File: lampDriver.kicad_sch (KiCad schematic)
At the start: 49 parts, among them IC8 FAN3100TSX, T4 NMOS_GDS-KS_SMD, U1 OPA2356AIDGKR, U3 LM2903, U4 AZ431LANTR

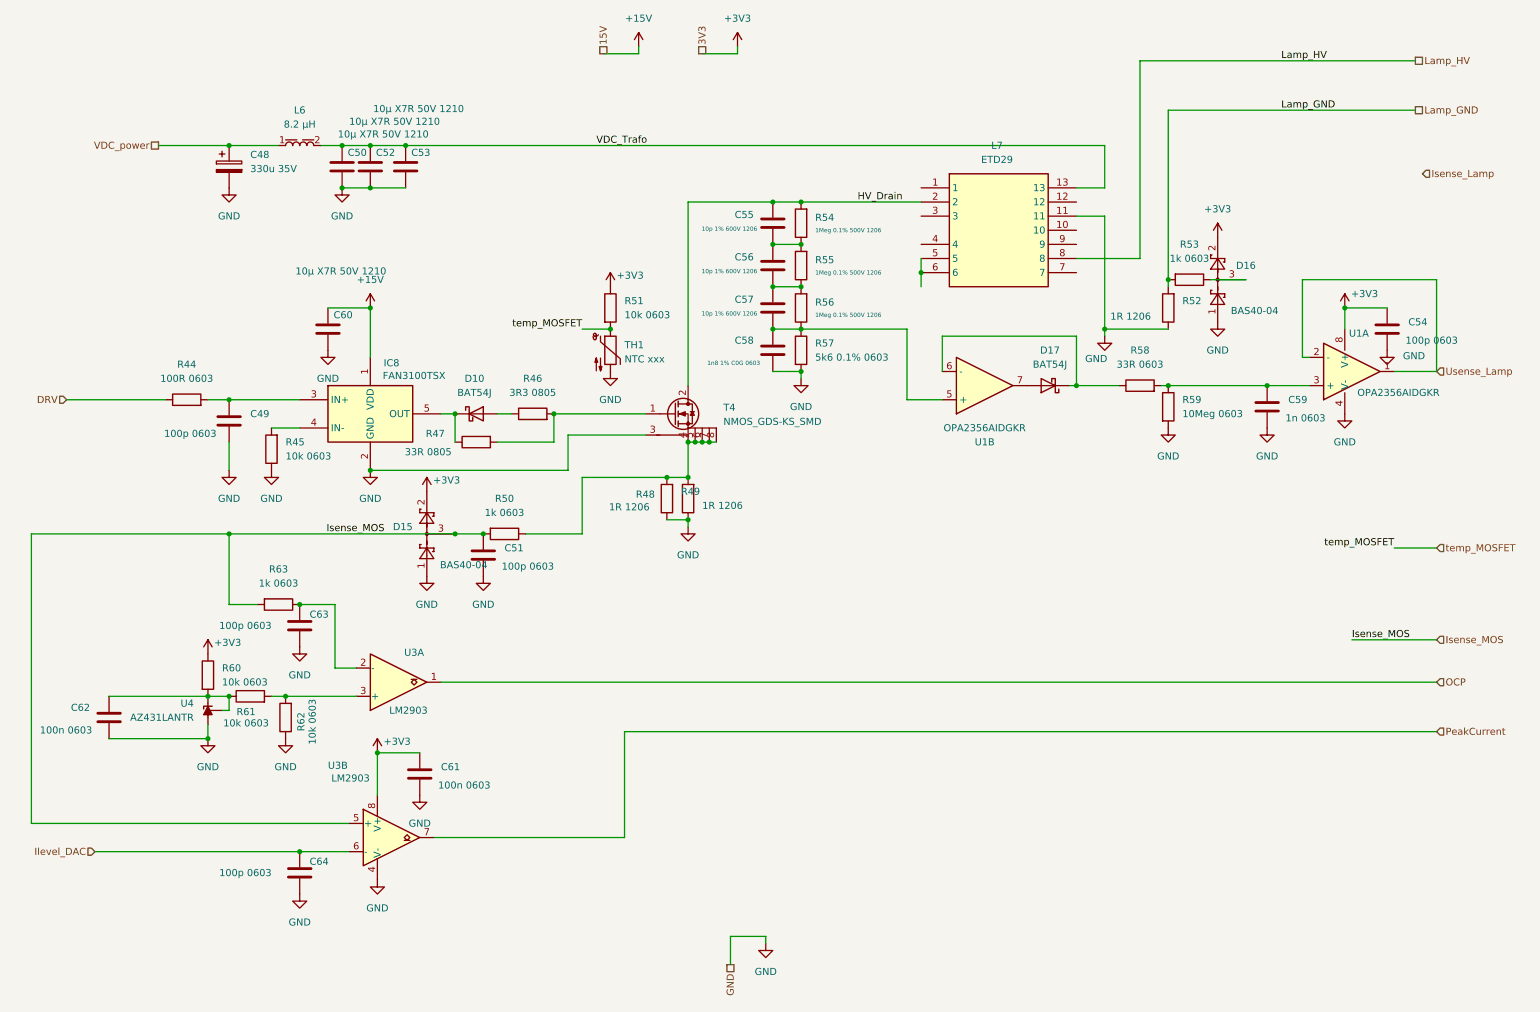
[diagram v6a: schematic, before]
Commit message: new current control V1
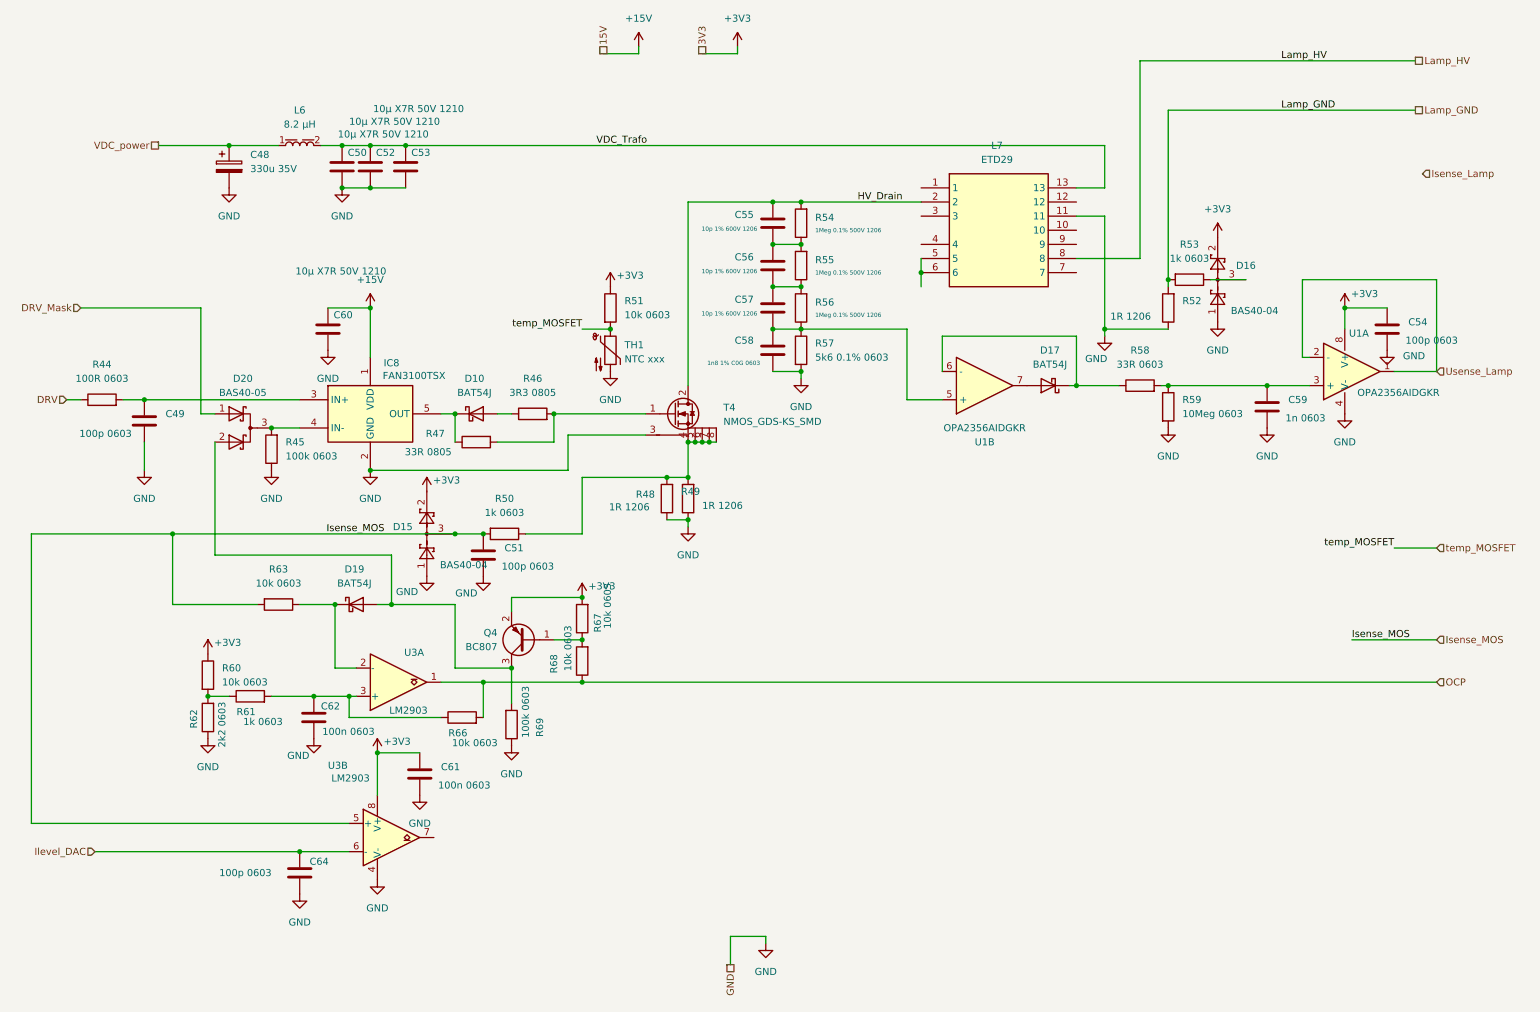
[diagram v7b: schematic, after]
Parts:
- removed C63: 100p 0603, Capacitor_SMD:C_0603_1608Metric, symbol Device:C
- removed U4: AZ431LANTR, Package_TO_SOT_SMD:SOT-23, symbol Reference_Voltage:TL432DBZ
- added D19: BAT54J, Diode_SMD:D_SOD-323F, symbol Diode:BAT54J
- added D20: BAS40-05, Package_TO_SOT_SMD:SOT-23, symbol Device:D_Schottky_Dual_CommonCathode_AAK_Parallel
- added Q4: BC807, Package_TO_SOT_SMD:SOT-23, symbol Transistor_BJT:Q_PNP_BEC
- added R66, R67, R68: 10k 0603, Resistor_SMD:R_0603_1608Metric, symbol Device:R
- added R69: 100k 0603, Resistor_SMD:R_0603_1608Metric, symbol Device:R
- R45: value 10k 0603 -> 100k 0603
- R61: value 10k 0603 -> 1k 0603
- R62: value 10k 0603 -> 2k2 0603
- R63: value 1k 0603 -> 10k 0603
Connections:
- net +3V3: now also Q4.2 (E), R67.2
- net GND: now also R69.1
- net OCP: now also R66.2, R68.1
- net at IC8.4 (IN-), R45.2: now also D20.3 (K)
- net at R60.2, R61.1: now also R62.2; no longer C62.1
- net at R61.2, U3.3 (+): now also C62.1, R66.1; no longer R62.2
- net at R63.1, U3.2 (-): now also D19.1 (K)
- net PeakCurrent: no longer names the net of U3.7
- new net: Q4.1 (B), R67.1, R68.2
- new net: D19.2 (A), D20.2 (A), Q4.3 (C), R69.2
- new net DRV_Mask: D20.1 (A)
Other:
- moved on the sheet: C49, C62, R44, R62
